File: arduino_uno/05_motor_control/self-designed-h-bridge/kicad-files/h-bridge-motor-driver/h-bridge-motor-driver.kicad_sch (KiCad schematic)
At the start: 16 parts, among them J1 Conn_01x05_Pin, J2 Conn_01x02_Pin, Q1 IRF9540N, Q2 IRLIZ44N, Q3 IRF9540N, Q4 IRLIZ44N, Q5 BC547, Q6 BC547

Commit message: add wago clamp
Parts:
- added J3, J4: 2601-3102, CONN2_2601-3102_WAG, symbol Wago 2601-3102:2601-3102
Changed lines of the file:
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@@
+	)
+	(symbol
+		(lib_id "Wago 2601-3102:2601-3102")
+		(at 194.31 88.9 0)
+		(unit 1)
+		(exclude_from_sim no)
+		(in_bom yes)
+		(on_board yes)
+		(dnp no)
+		(fields_autoplaced yes)
+		(property "Reference" "J3"
+			(at 208.28 91.4399 0)
+			(effects
+				(font
+					(size 1.524 1.524)
+				)
+				(justify left)
+			)
+		)
+		(property "Value" "2601-3102"
+			(at 208.28 93.9799 0)
+			(effects
+				(font
+					(size 1.524 1.524)
+				)
+				(justify left)
+			)
+		)
+		(property "Footprint" "CONN2_2601-3102_WAG"
+			(at 194.31 88.9 0)
+			(effects
+				(font
+					(size 1.27 1.27)
+					(italic yes)
+				)
+				(hide yes)
+			)
+		)
+		(property "Datasheet" "2601-3102"
+			(at 194.31 88.9 0)
+			(effects
+				(font
+					(size 1.27 1.27)
+					(italic yes)
+				)
+				(hide yes)
+			)
+		)
+		(property "Description" ""
+			(at 194.31 88.9 0)
+			(effects
+				(font
+					(size 1.27 1.27)
+				)
+				(hide yes)
+			)
+		)
+		(pin "3"
+		)
+		(pin "1"
+		)
+		(pin "4"
+		)
+		(pin "2"
+		)
+		(instances
+			(project ""
+				(path "/c86b6916-14ad-4ba0-a61b-f63bb8896688"
+					(reference "J3")
+					(unit 1)
+				)
+			)
+		)
 	)
 	(symbol
@@
 					(unit 1)
 				)
+			)
+		)
+	)
+	(symbol
+		(lib_id "Wago 2601-3102:2601-3102")
+		(at 31.75 76.2 0)
+		(unit 1)
+		(exclude_from_sim no)
+		(in_bom yes)
+		(on_board yes)
+		(dnp no)
+		(fields_autoplaced yes)
+		(property "Reference" "J4"
+			(at 45.72 78.7399 0)
+			(effects
+				(font
+					(size 1.524 1.524)
+				)
+				(justify left)
+			)
+		)
+		(property "Value" "2601-3102"
+			(at 45.72 81.2799 0)
+			(effects
+				(font
+					(size 1.524 1.524)
+				)
+				(justify left)
+			)
+		)
+		(property "Footprint" "CONN2_2601-3102_WAG"
+			(at 31.75 76.2 0)
+			(effects
+				(font
+					(size 1.27 1.27)
+					(italic yes)
+				)
+				(hide yes)
+			)
+		)
+		(property "Datasheet" "2601-3102"
+			(at 31.75 76.2 0)
+			(effects
+				(font
+					(size 1.27 1.27)
+					(italic yes)
+				)
+				(hide yes)
+			)
+		)
+		(property "Description" ""
+			(at 31.75 76.2 0)
+			(effects
+				(font
+					(size 1.27 1.27)
+				)
+				(hide yes)
+			)
+		)
+		(pin "3"
+		)
+		(pin "2"
+		)
+		(pin "4"
+		)
+		(pin "1"
+		)
+		(instances
+			(project ""
+				(path "/c86b6916-14ad-4ba0-a61b-f63bb8896688"
+					(reference "J4")
+					(unit 1)
+				)

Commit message: rework schematic
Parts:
- removed J2: Conn_01x02_Pin, symbol Connector:Conn_01x02_Pin
- added R5, R6, R7, R8: R, symbol Device:R
- J3, J4: footprint CONN2_2601-3102_WAG -> WAGO 2601-3102:CONN2_2601-3102_WAG
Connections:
- net GND is gone; now on an unnamed net: J1.5 (Pin_5)
- net at D2.1 (K): now also D1.1 (K), J4.1 (1_1), J4.2 (1_2), Q1.3 (S), Q3.3 (S), R2.1, R3.1
- net at D2.2 (A): now also D4.1 (K), J3.3 (2_1), J3.4 (2_2), Q3.2 (D), Q4.2 (D)
- net at Q3.1 (G): now also R3.2, R6.2
- net at Q4.1 (G): now also J1.4 (Pin_4), R8.1
- net at Q4.3 (S): now also D3.2 (A), D4.2 (A), J4.3 (2_1), J4.4 (2_2), Q2.3 (S), Q5.3 (E), Q6.3 (E), R7.2, R8.2
- net at Q1.1 (G), R2.2: now also R5.2; no longer Q5.1 (C)
- net at Q5.2 (B): now also R1.2; no longer R1.1
- net at J1.1 (Pin_1): now also R1.1; no longer R1.2
- net at J1.2 (Pin_2): now also Q2.1 (G), R7.1; no longer R4.2
- net at J1.3 (Pin_3): now also R4.1
- net at Q6.1 (C): now also R6.1
- net at Q6.2 (B): now also R4.2; no longer R4.1
- net at Q2.2 (D): now also D1.2 (A), D3.1 (K), J3.1 (1_1), J3.2 (1_2), Q1.2 (D)
- new net: Q5.1 (C), R5.1
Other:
- moved on the sheet: D1, D2, D3, D4, J1, J3, J4, Q1, Q2, Q3, Q4, Q5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

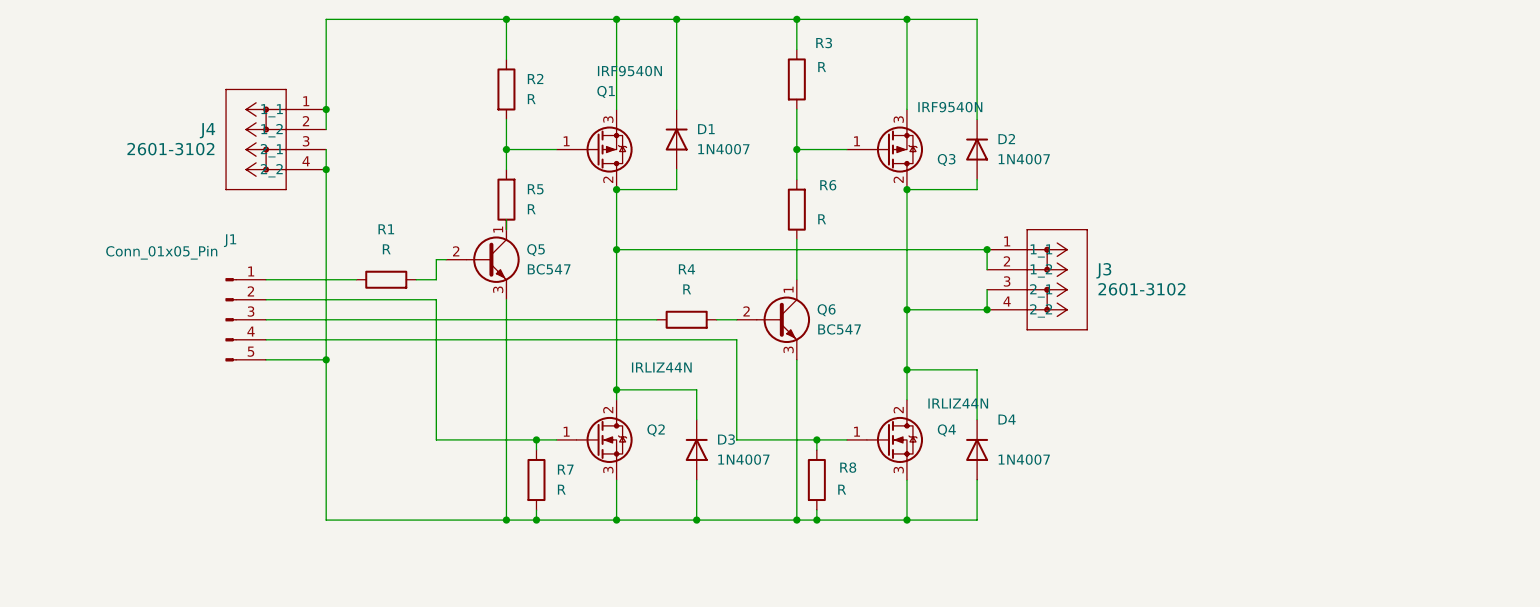
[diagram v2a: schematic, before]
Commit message: move fritzing files add footprints to parts
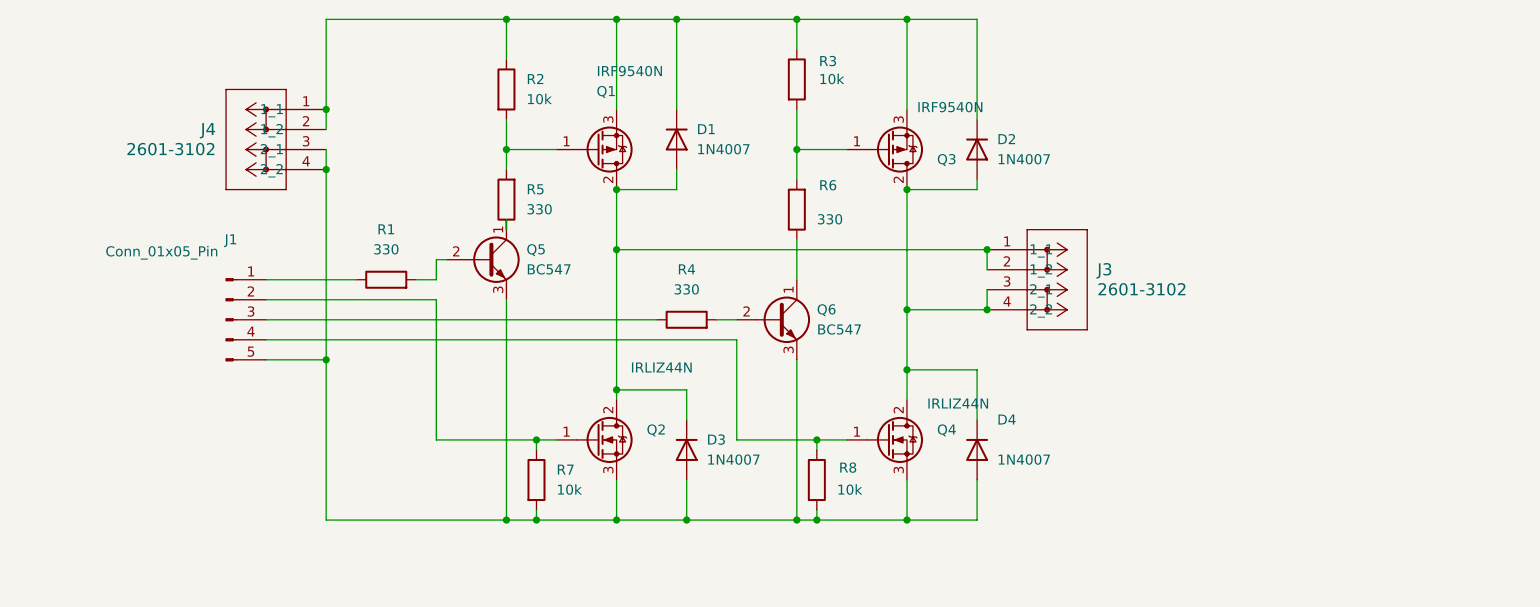
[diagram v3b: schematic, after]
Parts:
- J1: footprint (none) -> Connector_PinHeader_2.54mm:PinHeader_1x05_P2.54mm_Vertical
- R1, R4, R5, R6: value R -> 330; footprint (none) -> Resistor_THT:R_Axial_DIN0207_L6.3mm_D2.5mm_P10.16mm_Horizontal
- R2, R3, R7, R8: value R -> 10k; footprint (none) -> Resistor_THT:R_Axial_DIN0207_L6.3mm_D2.5mm_P10.16mm_Horizontal
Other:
- moved on the sheet: D3
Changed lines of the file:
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@@
+	)
+	(junction
+		(at 116.84 110.49)
+		(diameter 0)
+		(color 0 0 0 0)
 	)
 	(junction
@@
 	)
 	(junction
-		(at 118.11 110.49)
-		(diameter 0)
-		(color 0 0 0 0)
-	)
-	(junction
 		(at 107.95 68.58)
 		(diameter 0)
@@
 	(wire
 		(pts
-			(xy 118.11 105.41) (xy 118.11 110.49)
+			(xy 116.84 105.41) (xy 116.84 110.49)
 		)
 		(stroke
@@
 	(wire
 		(pts
+			(xy 116.84 110.49) (xy 107.95 110.49)
+		)
+		(stroke
+			(width 0)
+			(type default)
+		)
+	)
+	(wire
+		(pts
 			(xy 130.81 46.99) (xy 144.78 46.99)
 		)
@@
 	(wire
 		(pts
-			(xy 118.11 110.49) (xy 107.95 110.49)
-		)
-		(stroke
-			(width 0)
-			(type default)
-		)
-	)
-	(wire
-		(pts
 			(xy 144.78 105.41) (xy 144.78 110.49)
 		)
@@
 	(wire
 		(pts
-			(xy 118.11 93.98) (xy 107.95 93.98)
+			(xy 116.84 93.98) (xy 107.95 93.98)
 		)
 		(stroke
@@
 	(wire
 		(pts
-			(xy 118.11 97.79) (xy 118.11 93.98)
+			(xy 116.84 97.79) (xy 116.84 93.98)
 		)
 		(stroke
@@
 	(wire
 		(pts
+			(xy 116.84 110.49) (xy 130.81 110.49)
+		)
+		(stroke
+			(width 0)
+			(type default)
+		)
+	)
+	(wire
+		(pts
 			(xy 115.57 68.58) (xy 107.95 68.58)
 		)
@@
 		(pts
 			(xy 144.78 83.82) (xy 154.94 83.82)
-		)
-		(stroke
-			(width 0)
-			(type default)
-		)
-	)
-	(wire
-		(pts
-			(xy 130.81 110.49) (xy 118.11 110.49)
 		)
 		(stroke
@@
 			)
 		)
-		(property "Value" "R"
+		(property "Value" "10k"
 			(at 100.33 106.6799 0)
 			(effects
@@
 			)
 		)
-		(property "Footprint" ""
+		(property "Footprint" "Resistor_THT:R_Axial_DIN0207_L6.3mm_D2.5mm_P10.16mm_Horizontal"
 			(at 96.012 105.41 90)
 			(effects
@@
 			)
 		)
-		(property "Value" "R"
+		(property "Value" "330"
 			(at 96.52 71.1199 0)
 			(effects
@@
 			)
 		)
-		(property "Footprint" ""
+		(property "Footprint" "Resistor_THT:R_Axial_DIN0207_L6.3mm_D2.5mm_P10.16mm_Horizontal"
 			(at 95.758 69.85 90)
 			(effects
@@
 			)
 		)
-		(property "Footprint" ""
+		(property "Footprint" "Connector_PinHeader_2.54mm:PinHeader_1x05_P2.54mm_Vertical"
 			(at 58.42 85.09 0)
 			(effects
@@
 			)
 		)
-		(property "Value" "R"
+		(property "Value" "10k"
 			(at 135.89 106.6799 0)
 			(effects
@@
 			)
 		)
-		(property "Footprint" ""
+		(property "Footprint" "Resistor_THT:R_Axial_DIN0207_L6.3mm_D2.5mm_P10.16mm_Horizontal"
 			(at 131.572 105.41 90)
 			(effects
@@
 			)
 		)
-		(property "Value" "R"
+		(property "Value" "10k"
 			(at 96.52 57.1499 0)
 			(effects
@@
 			)
 		)
-		(property "Footprint" ""
+		(property "Footprint" "Resistor_THT:R_Axial_DIN0207_L6.3mm_D2.5mm_P10.16mm_Horizontal"
 			(at 92.202 55.88 90)
 			(effects
@@
 			)
 		)
-		(property "Value" "R"
+		(property "Value" "330"
 			(at 133.35 72.3899 0)
 			(effects
@@
 			)
 		)
-		(property "Footprint" ""
+		(property "Footprint" "Resistor_THT:R_Axial_DIN0207_L6.3mm_D2.5mm_P10.16mm_Horizontal"
 			(at 132.588 71.12 90)
 			(effects
@@
 	(symbol
 		(lib_id "Diode:1N4007")
-		(at 118.11 101.6 270)
+		(at 116.84 101.6 270)
 		(unit 1)
 		(exclude_from_sim no)
@@
 		(fields_autoplaced yes)
 		(property "Reference" "D3"
-			(at 120.65 100.3299 90)
+			(at 119.38 100.3299 90)
 			(effects
 				(font
@@
 		)
 		(property "Value" "1N4007"
-			(at 120.65 102.8699 90)
+			(at 119.38 102.8699 90)
 			(effects
 				(font
@@
 		)
 		(property "Footprint" "Diode_THT:D_DO-41_SOD81_P10.16mm_Horizontal"
-			(at 113.665 101.6 0)
+			(at 112.395 101.6 0)
 			(effects
 				(font
@@
 		)
 		(property "Datasheet" "http://www.vishay.com/docs/88503/1n4001.pdf"
-			(at 118.11 101.6 0)
+			(at 116.84 101.6 0)
 			(effects
 				(font
@@
 		)
 		(property "Description" "1000V 1A General Purpose Rectifier Diode, DO-41"
-			(at 118.11 101.6 0)
+			(at 116.84 101.6 0)
 			(effects
 				(font
@@
 		)
 		(property "Sim.Device" "D"
-			(at 118.11 101.6 0)
+			(at 116.84 101.6 0)
 			(effects
 				(font
@@
 		)
 		(property "Sim.Pins" "1=K 2=A"
-			(at 118.11 101.6 0)
+			(at 116.84 101.6 0)
 			(effects
 				(font
@@
 			)
 		)
-		(property "Value" "R"
+		(property "Value" "330"
 			(at 116.84 81.28 90)
 			(effects
@@
 			)
 		)
-		(property "Footprint" ""
+		(property "Footprint" "Resistor_THT:R_Axial_DIN0207_L6.3mm_D2.5mm_P10.16mm_Horizontal"
 			(at 116.84 86.868 90)
 			(effects
@@
 			)
 		)
-		(property "Value" "R"
+		(property "Value" "330"
 			(at 78.74 76.2 90)
 			(effects
@@
 			)
 		)
-		(property "Footprint" ""
+		(property "Footprint" "Resistor_THT:R_Axial_DIN0207_L6.3mm_D2.5mm_P10.16mm_Horizontal"
 			(at 78.74 81.788 90)
 			(effects
@@
 		(dnp no)
 		(property "Reference" "R3"
-			(at 133.096 50.038 0)
-			(effects
-				(font
-					(size 1.27 1.27)
-				)
-				(justify left)
-			)
-		)
-		(property "Value" "R"
-			(at 133.35 53.086 0)
-			(effects
-				(font
-					(size 1.27 1.27)
-				)
-				(justify left)
-			)
-		)
-		(property "Footprint" ""
+			(at 133.604 52.324 0)
+			(effects
+				(font
+					(size 1.27 1.27)
+				)
+				(justify left)
+			)
+		)
+		(property "Value" "10k"
+			(at 133.604 54.61 0)
+			(effects
+				(font
+					(size 1.27 1.27)
+				)
+				(justify left)
+			)
+		)
+		(property "Footprint" "Resistor_THT:R_Axial_DIN0207_L6.3mm_D2.5mm_P10.16mm_Horizontal"
 			(at 129.032 54.61 90)
 			(effects

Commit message: start routing
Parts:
- removed J1: Conn_01x05_Pin, Connector_PinHeader_2.54mm:PinHeader_1x05_P2.54mm_Vertical, symbol Connector:Conn_01x05_Pin
- added J2: Conn_01x06_Pin, Connector_PinSocket_2.54mm:PinSocket_1x06_P2.54mm_Vertical, symbol Connector:Conn_01x06_Pin
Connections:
- net at D1.1 (K), D2.1 (K), J4.1 (1_1)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: now also J2.1 (Pin_1)
- net at Q4.1 (G), R8.1: now also J2.5 (Pin_5)
- net at D3.2 (A), D4.2 (A), J4.3 (2_1)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: now also J2.6 (Pin_6)
- net at Q2.1 (G), R7.1: now also J2.3 (Pin_3)
- net at R1.1: now also J2.2 (Pin_2)
- net at R4.1: now also J2.4 (Pin_4)
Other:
- moved on the sheet: J4
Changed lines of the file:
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@@
 	(paper "A4")
 	(junction
+		(at 66.04 60.96)
+		(diameter 0)
+		(color 0 0 0 0)
+	)
+	(junction
 		(at 97.79 100.33)
 		(diameter 0)
@@
 	)
 	(junction
-		(at 71.12 66.04)
-		(diameter 0)
-		(color 0 0 0 0)
-	)
-	(junction
 		(at 107.95 110.49)
 		(diameter 0)
@@
 	)
 	(junction
+		(at 63.5 66.04)
+		(diameter 0)
+		(color 0 0 0 0)
+	)
+	(junction
 		(at 107.95 93.98)
 		(diameter 0)
@@
 	(wire
 		(pts
+			(xy 58.42 87.63) (xy 123.19 87.63)
+		)
+		(stroke
+			(width 0)
+			(type default)
+		)
+	)
+	(wire
+		(pts
 			(xy 93.98 63.5) (xy 93.98 66.04)
 		)
@@
 	(wire
 		(pts
+			(xy 63.5 60.96) (xy 66.04 60.96)
+		)
+		(stroke
+			(width 0)
+			(type default)
+		)
+	)
+	(wire
+		(pts
 			(xy 85.09 77.47) (xy 85.09 80.01)
 		)
@@
 	(wire
 		(pts
+			(xy 63.5 58.42) (xy 71.12 58.42)
+		)
+		(stroke
+			(width 0)
+			(type default)
+		)
+	)
+	(wire
+		(pts
 			(xy 130.81 58.42) (xy 130.81 63.5)
 		)
@@
 	(wire
 		(pts
+			(xy 58.42 85.09) (xy 113.03 85.09)
+		)
+		(stroke
+			(width 0)
+			(type default)
+		)
+	)
+	(wire
+		(pts
 			(xy 130.81 63.5) (xy 137.16 63.5)
 		)
@@
 	(wire
 		(pts
+			(xy 58.42 82.55) (xy 85.09 82.55)
+		)
+		(stroke
+			(width 0)
+			(type default)
+		)
+	)
+	(wire
+		(pts
 			(xy 97.79 101.6) (xy 97.79 100.33)
 		)
@@
 	(wire
 		(pts
+			(xy 58.42 90.17) (xy 71.12 90.17)
+		)
+		(stroke
+			(width 0)
+			(type default)
+		)
+	)
+	(wire
+		(pts
 			(xy 85.09 100.33) (xy 97.79 100.33)
 		)
@@
 	(wire
 		(pts
+			(xy 63.5 66.04) (xy 71.12 66.04)
+		)
+		(stroke
+			(width 0)
+			(type default)
+		)
+	)
+	(wire
+		(pts
 			(xy 154.94 76.2) (xy 154.94 78.74)
 		)
@@
 	(wire
 		(pts
+			(xy 66.04 60.96) (xy 66.04 77.47)
+		)
+		(stroke
+			(width 0)
+			(type default)
+		)
+	)
+	(wire
+		(pts
 			(xy 116.84 110.49) (xy 107.95 110.49)
 		)
@@
 	(wire
 		(pts
-			(xy 63.5 90.17) (xy 71.12 90.17)
-		)
-		(stroke
-			(width 0)
-			(type default)
-		)
-	)
-	(wire
-		(pts
 			(xy 144.78 105.41) (xy 144.78 110.49)
 		)
@@
 	(wire
 		(pts
-			(xy 63.5 80.01) (xy 74.93 80.01)
-		)
-		(stroke
-			(width 0)
-			(type default)
-		)
-	)
-	(wire
-		(pts
-			(xy 63.5 85.09) (xy 113.03 85.09)
+			(xy 58.42 77.47) (xy 66.04 77.47)
 		)
 		(stroke
@@
 	(wire
 		(pts
-			(xy 71.12 58.42) (xy 71.12 60.96)
-		)
-		(stroke
-			(width 0)
-			(type default)
-		)
-	)
-	(wire
-		(pts
 			(xy 144.78 46.99) (xy 153.67 46.99)
 		)
@@
 	(wire
 		(pts
-			(xy 63.5 82.55) (xy 85.09 82.55)
-		)
-		(stroke
-			(width 0)
-			(type default)
-		)
-	)
-	(wire
-		(pts
 			(xy 116.84 93.98) (xy 107.95 93.98)
 		)
@@
 	(wire
 		(pts
-			(xy 71.12 63.5) (xy 71.12 66.04)
+			(xy 63.5 63.5) (xy 63.5 66.04)
 		)
 		(stroke
@@
 	(wire
 		(pts
+			(xy 71.12 60.96) (xy 71.12 58.42)
+		)
+		(stroke
+			(width 0)
+			(type default)
+		)
+	)
+	(wire
+		(pts
+			(xy 66.04 60.96) (xy 71.12 60.96)
+		)
+		(stroke
+			(width 0)
+			(type default)
+		)
+	)
+	(wire
+		(pts
 			(xy 144.78 110.49) (xy 133.35 110.49)
 		)
@@
 	(wire
 		(pts
-			(xy 63.5 87.63) (xy 123.19 87.63)
+			(xy 58.42 80.01) (xy 74.93 80.01)
 		)
 		(stroke
@@
 	)
 	(symbol
-		(lib_id "Connector:Conn_01x05_Pin")
-		(at 58.42 85.09 0)
-		(unit 1)
-		(exclude_from_sim no)
-		(in_bom yes)
-		(on_board yes)
-		(dnp no)
-		(property "Reference" "J1"
-			(at 59.055 74.93 0)
-			(effects
-				(font
-					(size 1.27 1.27)
-				)
-			)
-		)
-		(property "Value" "Conn_01x05_Pin"
-			(at 50.292 76.454 0)
-			(effects
-				(font
-					(size 1.27 1.27)
-				)
-			)
-		)
-		(property "Footprint" "Connector_PinHeader_2.54mm:PinHeader_1x05_P2.54mm_Vertical"
-			(at 58.42 85.09 0)
-			(effects
-				(font
-					(size 1.27 1.27)
-				)
-				(hide yes)
-			)
-		)
-		(property "Datasheet" "~"
-			(at 58.42 85.09 0)
-			(effects
-				(font
-					(size 1.27 1.27)
-				)
-				(hide yes)
-			)
-		)
-		(property "Description" "Generic connector, single row, 01x05, script generated"
-			(at 58.42 85.09 0)
-			(effects
-				(font
-					(size 1.27 1.27)
-				)
-				(hide yes)
-			)
-		)
-		(pin "2"
-		)
-		(pin "5"
-		)
-		(pin "3"
-		)
-		(pin "1"
-		)
-		(pin "4"
-		)
-		(instances
-			(project ""
-				(path "/c86b6916-14ad-4ba0-a61b-f63bb8896688"
-					(reference "J1")
-					(unit 1)
-				)
-			)
-		)
-	)
-	(symbol
 		(lib_id "Transistor_BJT:BC547")
 		(at 128.27 85.09 0)
@@
 		(lib_name "2601-3102_1")
 		(lib_id "Wago 2601-3102:2601-3102")
-		(at 71.12 58.42 0)
+		(at 63.5 58.42 0)
 		(mirror y)
 		(unit 1)
@@
 		(dnp no)
 		(property "Reference" "J4"
-			(at 57.15 60.9599 0)
+			(at 49.53 60.9599 0)
 			(effects
 				(font
@@
 		)
 		(property "Value" "2601-3102"
-			(at 57.15 63.4999 0)
+			(at 49.53 63.4999 0)
 			(effects
 				(font
@@
 		)
 		(property "Footprint" "WAGO 2601-3102:CONN2_2601-3102_WAG"
-			(at 71.12 58.42 0)
+			(at 63.5 58.42 0)
 			(effects
 				(font
@@
 		)
 		(property "Datasheet" "2601-3102"
-			(at 71.12 58.42 0)
+			(at 63.5 58.42 0)
 			(effects
 				(font
@@
 		)
 		(property "Description" ""
-			(at 71.12 58.42 0)
+			(at 63.5 58.42 0)
 			(effects
 				(font
@@
 					(unit 1)
 				)
+			)
+		)
+	)
+	(symbol
+		(lib_id "Connector:Conn_01x06_Pin")
+		(at 53.34 82.55 0)
+		(unit 1)
+		(exclude_from_sim no)
+		(in_bom yes)
+		(on_board yes)
+		(dnp no)
+		(fields_autoplaced yes)
+		(property "Reference" "J2"
+			(at 53.975 72.39 0)
+			(effects
+				(font
+					(size 1.27 1.27)
+				)
+			)
+		)
+		(property "Value" "Conn_01x06_Pin"
+			(at 53.975 74.93 0)
+			(effects
+				(font
+					(size 1.27 1.27)
+				)
+			)
+		)
+		(property "Footprint" "Connector_PinSocket_2.54mm:PinSocket_1x06_P2.54mm_Vertical"
+			(at 53.34 82.55 0)
+			(effects
+				(font
+					(size 1.27 1.27)
+				)
+				(hide yes)
+			)
+		)
+		(property "Datasheet" "~"
+			(at 53.34 82.55 0)
+			(effects
+				(font
+					(size 1.27 1.27)
+				)
+				(hide yes)
+			)
+		)
+		(property "Description" "Generic connector, single row, 01x06, script generated"
+			(at 53.34 82.55 0)
+			(effects
+				(font
+					(size 1.27 1.27)
+				)
+				(hide yes)
+			)
+		)
+		(pin "4"
+		)
+		(pin "2"
+		)
+		(pin "3"
+		)
+		(pin "1"
+		)
+		(pin "5"
+		)
+		(pin "6"
+		)
+		(instances
+			(project ""
+				(path "/c86b6916-14ad-4ba0-a61b-f63bb8896688"
+					(reference "J2")
+					(unit 1)
+				)
